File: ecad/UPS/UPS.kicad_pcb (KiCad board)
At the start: 4 copper layers, 121.9 x 139.7 mm, 173 parts, among them J10 BOARD_10K_NTC, J11 BAT3_10K_NTC, J12 PI_UART, J2 BAT1_10K_NTC, J3 USB_C_Receptacle_USB2.0_16P, J4 PROG, J5 BAT2_10K_NTC, J6 BAT4_10K_NTC, J7 Fan_Connector, J8 PJ-002AH, J9 OLED_3V3_I2C2, Q1 CSD18540Q5B, Q2 Q_PMOS_DGS, Q3 IRLR7843TRPBF, Q4 Q_PMOS_DGS, Q5 CSD18540Q5B, Q6 CSD18540Q5B, Q7 CSD18540Q5B, Q8 2N7002, SW3 SW_DPDT_x2, U1 BQ25730RSNR, U2 MPQ5031GRE-0001-AEC1-P, U4 STM32L152RCT6, U5 AP2112K-3.3TRG1, U6 BOOT0, U7 NRST

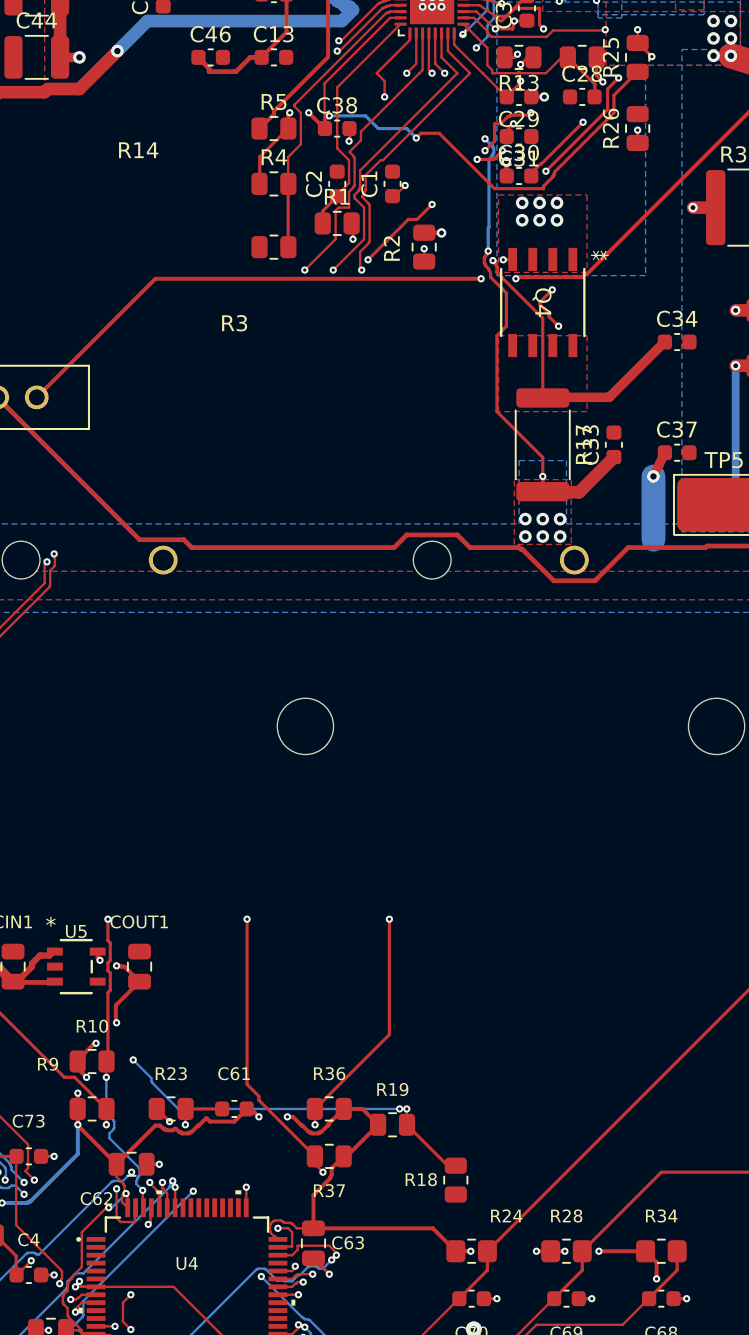
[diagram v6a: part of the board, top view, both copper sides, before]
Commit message: eh
Grounded the charger’s cell-count divider.
Corrected C9 from 470 pF to 470 nF.
Connected the STM’s unused LCD supply pin.
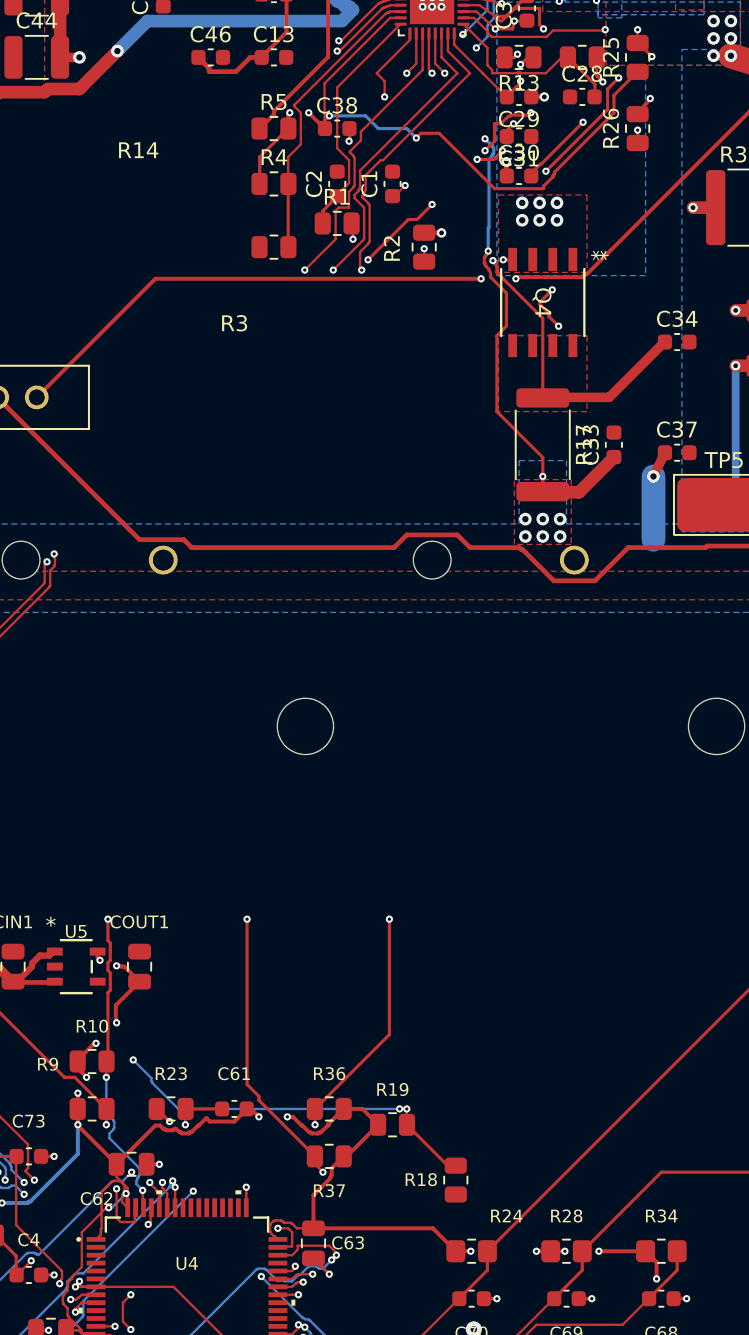
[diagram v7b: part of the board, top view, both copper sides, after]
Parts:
- C9: value 470pF -> 470nF
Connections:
- R26 pad 2: GNDA -> GND
- U4 pad 1: unconnected-(U4B-VLCD-Pad1) -> +3.3V
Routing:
- net +3.3V: track 251.3 -> 257.8 mm
- net GND: track 143.3 -> 144.6 mm, vias 116 -> 117
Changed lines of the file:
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@@
 			)
 		)
-		(property "Value" "470pF"
+		(property "Value" "470nF"
 			(at 1.8625 -3.3625 0)
 			(layer "F.Fab")
@@
 			(size 1.1938 0.3048)
 			(layers "F.Cu" "F.Mask" "F.Paste")
-			(net "unconnected-(U4B-VLCD-Pad1)")
+			(net "+3.3V")
 			(pinfunction "VLCD_1")
 			(pintype "free")
@@
 			(layers "F.Cu" "F.Mask" "F.Paste")
 			(roundrect_rratio 0.243902)
-			(net "GNDA")
+			(net "GND")
 			(pintype "passive")
 		)
@@
 	)
 	(segment
+		(start 96.3 134.6)
+		(end 96.35 134.55)
+		(width 0.15)
+		(layer "F.Cu")
+		(net "+3.3V")
+	)
+	(segment
 		(start 94.2 127.1)
 		(end 94.2 127.15)
@@
 	)
 	(segment
+		(start 95.55 137.95)
+		(end 95.55 137.6)
+		(width 0.15)
+		(layer "F.Cu")
+		(net "+3.3V")
+	)
+	(segment
 		(start 93.15 142.25)
 		(end 93.15 141.85)
@@
 	)
 	(segment
+		(start 95.55 137.6)
+		(end 95.6 137.55)
+		(width 0.15)
+		(layer "F.Cu")
+		(net "+3.3V")
+	)
+	(segment
 		(start 89.1 146.5)
 		(end 89.0875 146.5)
@@
 	)
 	(segment
+		(start 96.85 134.6)
+		(end 97.25 135)
+		(width 0.15)
+		(layer "F.Cu")
+		(net "+3.3V")
+	)
+	(segment
 		(start 51.8 134.4)
 		(end 51.85 134.35)
@@
 	)
 	(segment
+		(start 95.6 135.25)
+		(end 96.25 134.6)
+		(width 0.15)
+		(layer "F.Cu")
+		(net "+3.3V")
+	)
+	(segment
 		(start 51.8 124.95)
 		(end 51.85 124.9)
@@
 	)
 	(segment
+		(start 97.25 136.25)
+		(end 97.25 136.250001)
+		(width 0.15)
+		(layer "F.Cu")
+		(net "+3.3V")
+	)
+	(segment
 		(start 99.7 131.35)
 		(end 100.1 131.35)
@@
 	)
 	(segment
+		(start 96.8 134.6)
+		(end 96.85 134.6)
+		(width 0.15)
+		(layer "F.Cu")
+		(net "+3.3V")
+	)
+	(segment
 		(start 106.25 137.75)
 		(end 106.25 137.35)
@@
 	)
 	(segment
+		(start 97.25 135)
+		(end 97.25 136.25)
+		(width 0.15)
+		(layer "F.Cu")
+		(net "+3.3V")
+	)
+	(segment
 		(start 99 154.9)
 		(end 99 154.9125)
@@
 	)
 	(segment
+		(start 96.75 134.55)
+		(end 96.8 134.6)
+		(width 0.15)
+		(layer "F.Cu")
+		(net "+3.3V")
+	)
+	(segment
 		(start 94.0875 127)
 		(end 94.1 127)
@@
 	)
 	(segment
+		(start 95.25 138.25)
+		(end 95.55 137.95)
+		(width 0.15)
+		(layer "F.Cu")
+		(net "+3.3V")
+	)
+	(segment
 		(start 87.0875 138)
 		(end 87.1 138)
@@
 	)
 	(segment
+		(start 95.6 137.55)
+		(end 95.6 135.25)
+		(width 0.15)
+		(layer "F.Cu")
+		(net "+3.3V")
+	)
+	(segment
 		(start 97 134.8)
 		(end 97 134.75)
@@
 	)
 	(segment
+		(start 96.35 134.55)
+		(end 96.75 134.55)
+		(width 0.15)
+		(layer "F.Cu")
+		(net "+3.3V")
+	)
+	(segment
 		(start 89.1 146.5)
 		(end 89.25 146.35)
@@
 	)
 	(segment
+		(start 96.25 134.6)
+		(end 96.3 134.6)
+		(width 0.15)
+		(layer "F.Cu")
+		(net "+3.3V")
+	)
+	(segment
 		(start 113.1 131)
 		(end 112.1 130)
@@
 	)
 	(segment
+		(start 95.250001 138.25)
+		(end 95.25 138.25)
+		(width 0.15)
+		(layer "F.Cu")
+		(net "+3.3V")
+	)
+	(segment
 		(start 100.5 131.449999)
 		(end 100.55 131.449999)
@@
 	)
 	(segment
+		(start 129.5 67.0875)
+		(end 130.3 66.099999)
+		(width 0.25)
+		(layer "F.Cu")
+		(net "GND")
+	)
+	(segment
 		(start 97.5 149.5)
 		(end 97.45 149.55)
@@
 	)
 	(via
+		(at 130.3 66.099999)
+		(size 0.46)
+		(drill 0.2032)
+		(layers "F.Cu" "B.Cu")
+		(net "GND")
+	)
+	(via
 		(at 104.35 150.5)
 		(size 0.46)
@@
 		)
 	)
+	(group "23 Rebuilt MCU controls"
+		(members "288198d1-b2bd-4eaf-a29c-26afd91b8c08" "2d58a342-d6f0-410a-81e3-64797b39f099"
+			"4984ae29-bbf5-420d-8e0f-e398039a65fe" "4c867ef0-bb1f-43d2-913a-10c52c6e9b10"
+			"5cf79272-d955-4491-af65-cf488a6ffd7b" "9b10dbcb-1d13-4229-94f4-c107b8b05ea5"
+			"9ebd8b47-a38d-478a-80ad-a852efead124" "a0ea23c5-13cf-4df4-9455-60eaa6c76bd3"
+			"bc74a342-3f5a-4c9d-bbb2-8ee8a4572fe9" "cd84c712-45fb-4a07-9317-b990a9108d57"
+			"d9669044-7191-4ad3-8035-02ff49231963" "df9606fc-d56f-4ea3-93f3-4fab13c4484e"
+			"e11e5878-47ea-4be1-bd3c-1736c2b10d95" "ee1ab030-ac98-40d3-b10b-01bd77f2f803"
+		)
+	)
